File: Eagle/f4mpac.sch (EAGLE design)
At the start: 47 parts, among them CN1 DIP40 MB CONN, IC1 YM2413, IC10 27C128L, IC2 74LS30D, IC3 74LS04D, IC4 LM4558N, IC5 Z80, IC6 74LS30D, IC7 74LS02D, IC8 74LS74D, IC9 74LS125D

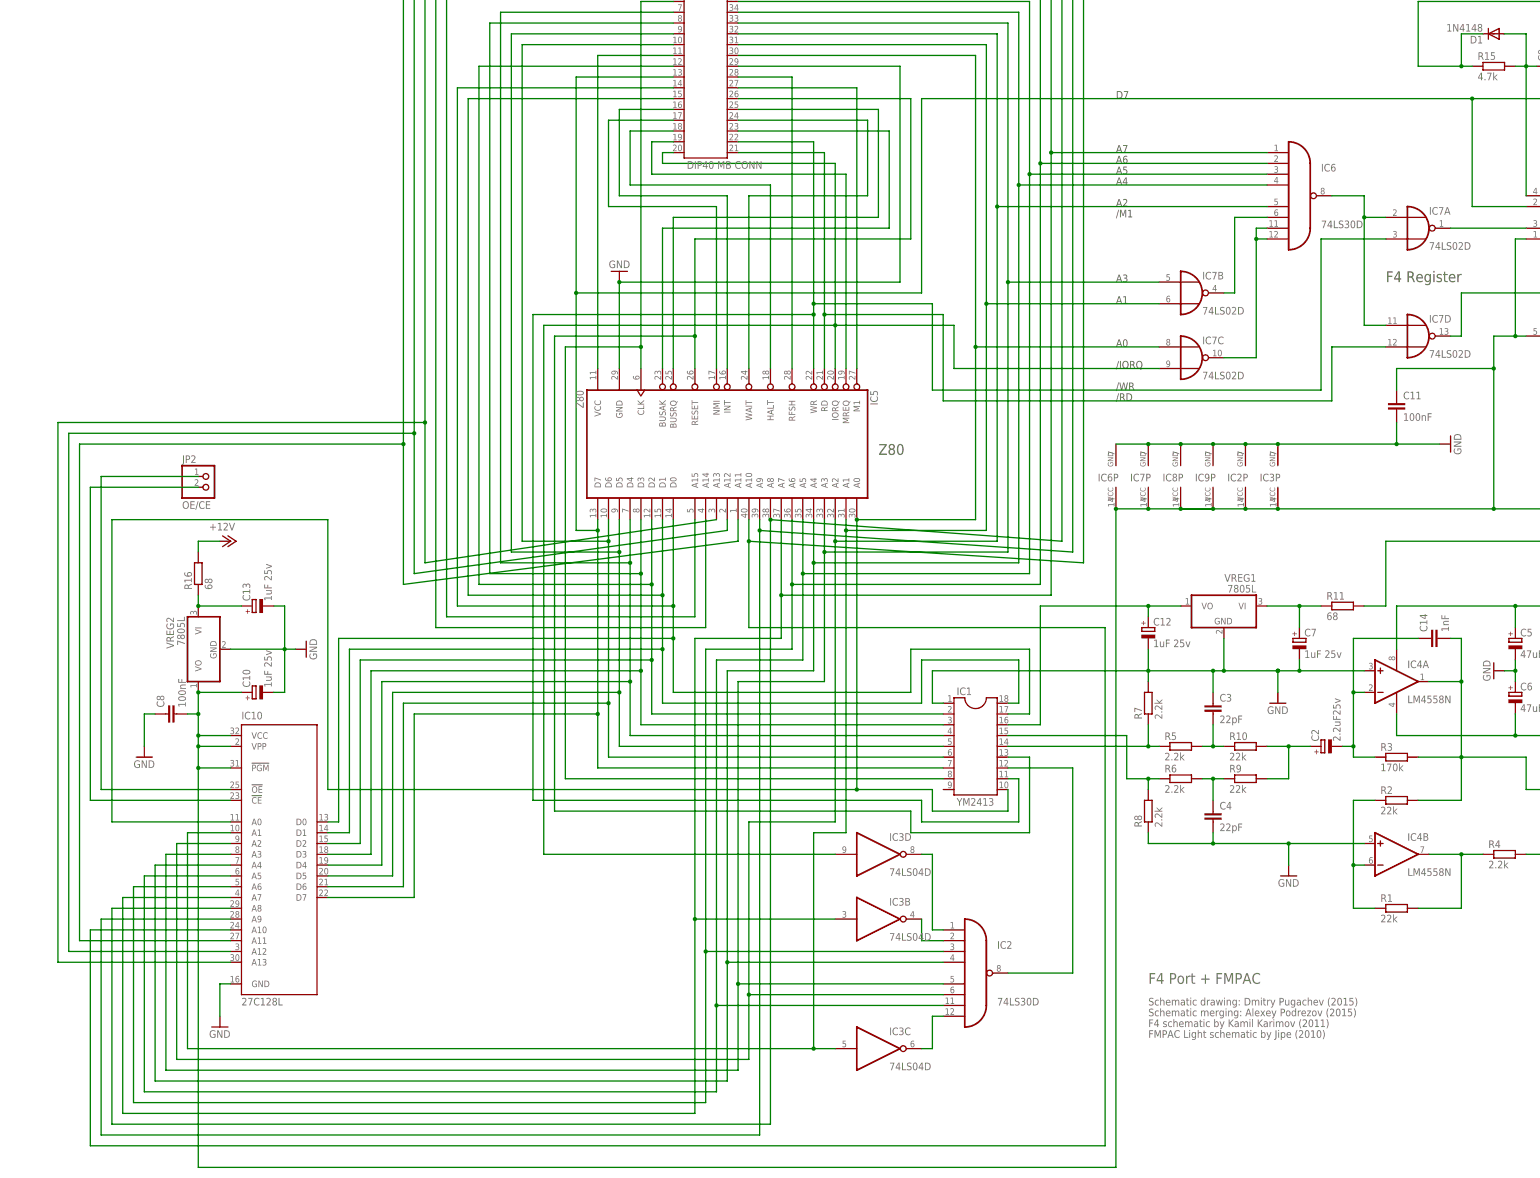
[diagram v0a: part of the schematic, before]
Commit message: New board version 1.3
New board version 1.3, new combined and selectable ROM, easier to get
ROM chip, corrected names error, blocking capacitors, additional noise
suppressing capacitor
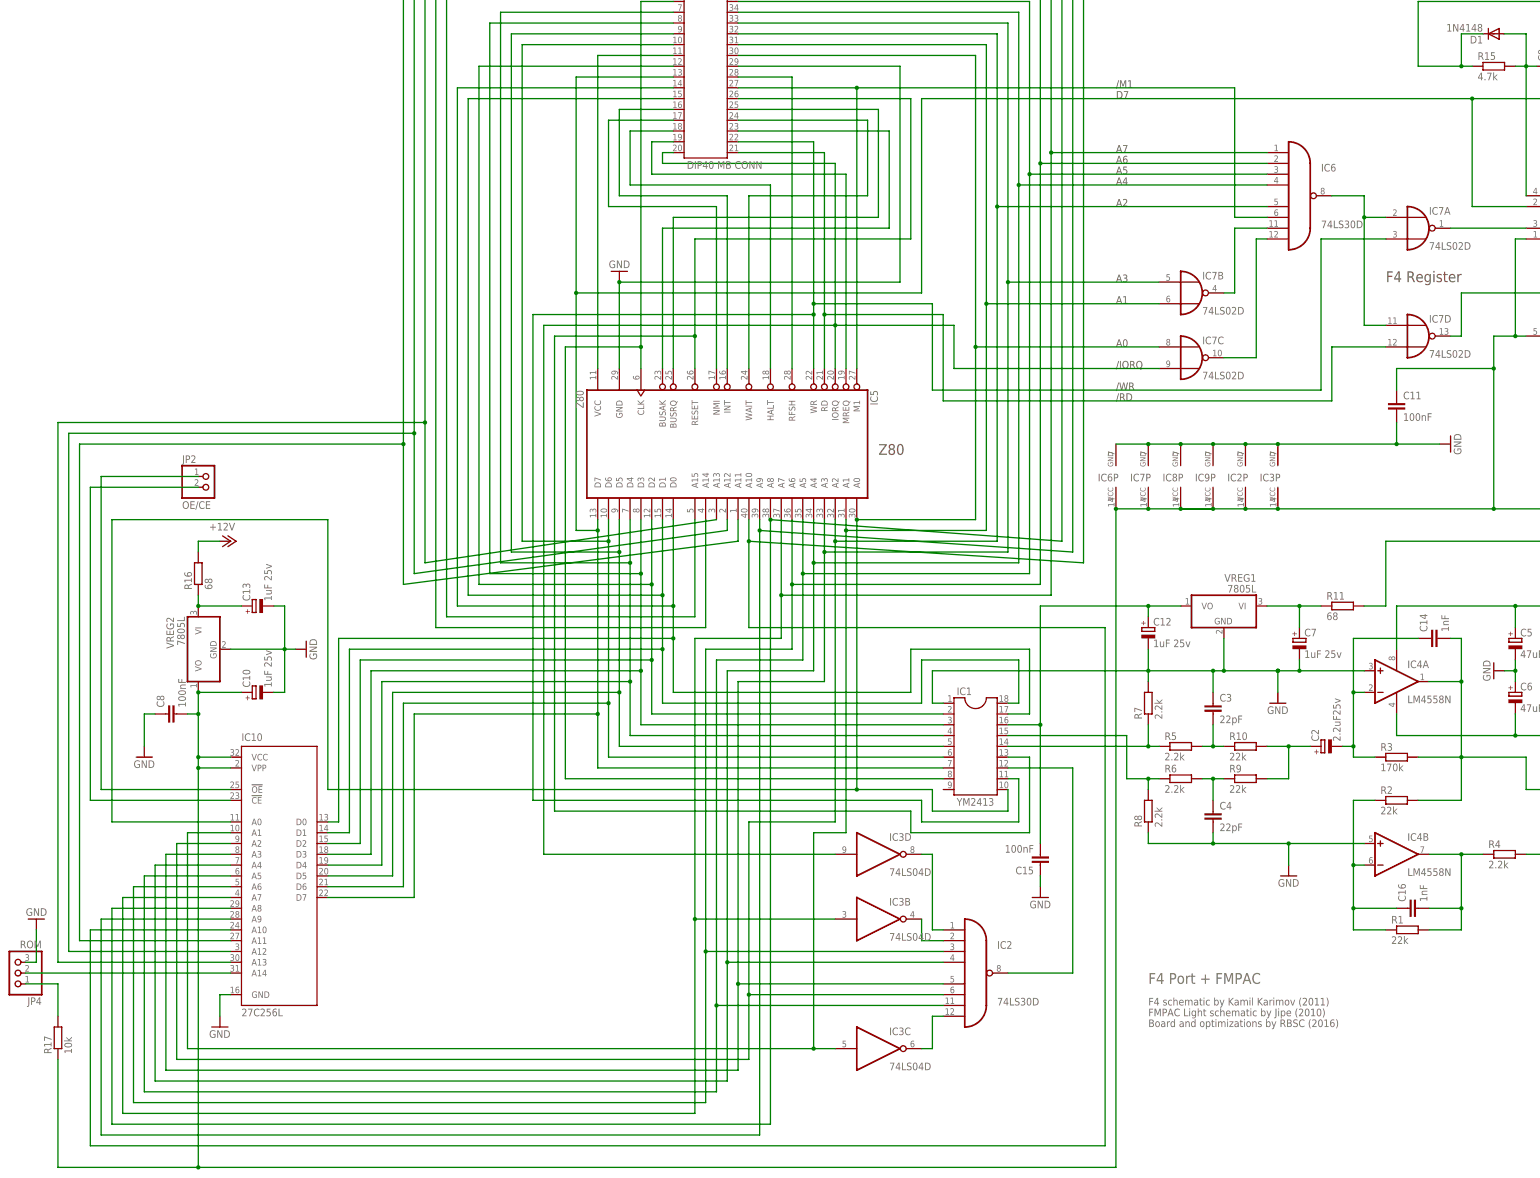
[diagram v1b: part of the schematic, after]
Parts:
- added C15: 100nF, rcl:C-EUC0805
- added C16: 1nF, rcl:C-EUC0805
- added JP4: ROM, pinhead:PINHD-1X3/90
- added R17: 10k, rcl:R-EU_R0805
- IC10: value 27C128L -> 27C256L; device microchip:27C128L -> microchip:27C256L
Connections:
- removed net N$10: IC4B.OUT, R1.2, R4.1
- removed net N$29: IC6A.I5, IC7B.O
- new net N$24: IC6A.I6, IC7B.O
- new net N$25: IC10.A14, JP4.2
- new net N$26: JP4.1, R17.2
- new net N$27: C16.2, IC4B.OUT, R1.2, R4.1
- net +5VREG: now also R17.1; no longer IC10.!PGM
- net GND: now also C15.1, JP4.3
- net M1: now also IC6A.I5
- net N$23: now also C15.2
- net N$30: no longer IC6A.I6
- net N$9: now also C16.1
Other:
- note added: "Board and optimizations by RBSC (2016)"
- note removed: "Schematic drawing: Dmitry Pugachev (2015)"
- note removed: "Schematic merging: Alexey Podrezov (2015)"
- moved on the sheet: IC10, R1

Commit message: Updated source and gerber files, added schematics
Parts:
- added SJ1, SJ2: (no value), jumper:SJ2W
- IC10: value 27C256L -> 27C512AL; device microchip:27C256L -> microchip:27C512AL
- JP4: value ROM -> ROMSEL; device pinhead:PINHD-1X3/90 -> pinhead:PINHD-1X2/90
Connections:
- new net N$10: IC10.A14, SJ1.2
- net +5VREG: now also SJ2.1; no longer IC10.VPP
- net A14: now also SJ1.3
- net A15: now also SJ2.3
- net GND: now also JP4.1; no longer JP4.3
- net N$20: now also IC10.VPP/!OE; no longer IC10.!OE
- net N$25: now also IC10.A15, SJ2.2; no longer IC10.A14, JP4.2
- net N$26: now also JP4.2, SJ1.1; no longer JP4.1
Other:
- moved on the sheet: IC10, R17
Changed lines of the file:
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@@
 <part name="GND12" library="supply1" deviceset="GND" device=""/>
 <part name="C14" library="rcl" deviceset="C-EU" device="C0805" value="1nF"/>
-<part name="IC10" library="microchip" deviceset="27*256" device="L" technology="C"/>
-<part name="R17" library="rcl" deviceset="R-EU_" device="R0805" value="10k"/>
-<part name="JP4" library="pinhead" deviceset="PINHD-1X3" device="/90" value="ROM"/>
-<part name="GND13" library="supply1" deviceset="GND" device=""/>
 <part name="C15" library="rcl" deviceset="C-EU" device="C0805" value="100nF"/>
 <part name="GND14" library="supply1" deviceset="GND" device=""/>
 <part name="C16" library="rcl" deviceset="C-EU" device="C0805" value="1nF"/>
+<part name="IC10" library="microchip" deviceset="27*512A" device="L" technology="C"/>
+<part name="SJ2" library="jumper" deviceset="SJ2W" device=""/>
+<part name="SJ1" library="jumper" deviceset="SJ2W" device=""/>
+<part name="JP4" library="pinhead" deviceset="PINHD-1X2" device="/90" value="ROMSEL"/>
+<part name="GND13" library="supply1" deviceset="GND" device=""/>
+<part name="R17" library="rcl" deviceset="R-EU_" device="R0805" value="10k"/>
 </parts>
 <sheets>
@@
 <instance part="GND12" gate="1" x="-129.54" y="48.26"/>
 <instance part="C14" gate="G$1" x="172.72" y="76.2" rot="R90"/>
-<instance part="IC10" gate="G$1" x="-99.06" y="20.32"/>
-<instance part="R17" gate="G$1" x="-149.86" y="-17.78" rot="R90"/>
-<instance part="JP4" gate="A" x="-160.02" y="-2.54" rot="R180"/>
-<instance part="GND13" gate="1" x="-154.94" y="10.16" rot="R180"/>
 <instance part="C15" gate="G$1" x="81.28" y="22.86" rot="R180"/>
 <instance part="GND14" gate="1" x="81.28" y="15.24"/>
 <instance part="C16" gate="G$1" x="167.64" y="12.7" rot="R90"/>
+<instance part="IC10" gate="G$1" x="-99.06" y="17.78"/>
+<instance part="SJ2" gate="G$1" x="-172.72" y="-17.78" rot="R180"/>
+<instance part="SJ1" gate="G$1" x="-157.48" y="43.18" rot="R180"/>
+<instance part="JP4" gate="G$1" x="-167.64" y="15.24" rot="R180"/>
+<instance part="GND13" gate="1" x="-162.56" y="-7.62"/>
+<instance part="R17" gate="G$1" x="-157.48" y="2.54" rot="R90"/>
 </instances>
 <busses>
@@
 </segment>
 <segment>
-<pinref part="IC10" gate="G$1" pin="GND"/>
-<pinref part="GND10" gate="1" pin="GND"/>
-<wire x1="-109.22" y1="-7.62" x2="-111.76" y2="-7.62" width="0.1524" layer="91"/>
-<wire x1="-111.76" y1="-7.62" x2="-111.76" y2="-12.7" width="0.1524" layer="91"/>
-</segment>
-<segment>
-<pinref part="JP4" gate="A" pin="3"/>
-<wire x1="-157.48" y1="0" x2="-154.94" y2="0" width="0.1524" layer="91"/>
-<wire x1="-154.94" y1="0" x2="-154.94" y2="7.62" width="0.1524" layer="91"/>
-<pinref part="GND13" gate="1" pin="GND"/>
-</segment>
-<segment>
 <pinref part="GND14" gate="1" pin="GND"/>
 <pinref part="C15" gate="G$1" pin="1"/>
 <wire x1="81.28" y1="17.78" x2="81.28" y2="20.32" width="0.1524" layer="91"/>
+</segment>
+<segment>
+<pinref part="IC10" gate="G$1" pin="GND"/>
+<pinref part="GND10" gate="1" pin="GND"/>
+<wire x1="-109.22" y1="-10.16" x2="-111.76" y2="-10.16" width="0.1524" layer="91"/>
+<wire x1="-111.76" y1="-10.16" x2="-111.76" y2="-12.7" width="0.1524" layer="91"/>
+</segment>
+<segment>
+<pinref part="JP4" gate="G$1" pin="1"/>
+<wire x1="-165.1" y1="12.7" x2="-162.56" y2="12.7" width="0.1524" layer="91"/>
+<wire x1="-162.56" y1="12.7" x2="-162.56" y2="-5.08" width="0.1524" layer="91"/>
+<pinref part="GND13" gate="1" pin="GND"/>
 </segment>
 </net>
@@
 <wire x1="0" y1="104.14" x2="0" y2="81.28" width="0.1524" layer="91"/>
 <wire x1="0" y1="81.28" x2="-58.42" y2="81.28" width="0.1524" layer="91"/>
-<wire x1="-58.42" y1="81.28" x2="-58.42" y2="228.6" width="0.1524" layer="91"/>
 <pinref part="CN1" gate="G$1" pin="5"/>
+<wire x1="-58.42" y1="81.28" x2="-58.42" y2="132.08" width="0.1524" layer="91"/>
+<wire x1="-58.42" y1="132.08" x2="-58.42" y2="228.6" width="0.1524" layer="91"/>
 <wire x1="-58.42" y1="228.6" x2="-5.08" y2="228.6" width="0.1524" layer="91"/>
+<wire x1="-58.42" y1="132.08" x2="-172.72" y2="132.08" width="0.1524" layer="91"/>
+<wire x1="-172.72" y1="132.08" x2="-172.72" y2="-12.7" width="0.1524" layer="91"/>
+<junction x="-58.42" y="132.08"/>
+<pinref part="SJ2" gate="G$1" pin="3"/>
 </segment>
 </net>
@@
 <wire x1="2.54" y1="104.14" x2="2.54" y2="78.74" width="0.1524" layer="91"/>
 <wire x1="2.54" y1="78.74" x2="-60.96" y2="78.74" width="0.1524" layer="91"/>
-<wire x1="-60.96" y1="78.74" x2="-60.96" y2="231.14" width="0.1524" layer="91"/>
+<wire x1="-60.96" y1="78.74" x2="-60.96" y2="129.54" width="0.1524" layer="91"/>
 <pinref part="CN1" gate="G$1" pin="4"/>
+<wire x1="-60.96" y1="129.54" x2="-60.96" y2="231.14" width="0.1524" layer="91"/>
 <wire x1="-60.96" y1="231.14" x2="-5.08" y2="231.14" width="0.1524" layer="91"/>
+<wire x1="-60.96" y1="129.54" x2="-152.4" y2="129.54" width="0.1524" layer="91"/>
+<wire x1="-152.4" y1="129.54" x2="-152.4" y2="53.34" width="0.1524" layer="91"/>
+<junction x="-60.96" y="129.54"/>
+<pinref part="SJ1" gate="G$1" pin="3"/>
+<wire x1="-152.4" y1="53.34" x2="-157.48" y2="53.34" width="0.1524" layer="91"/>
+<wire x1="-157.48" y1="53.34" x2="-157.48" y2="48.26" width="0.1524" layer="91"/>
 </segment>
 </net>
@@
 <wire x1="-116.84" y1="-48.26" x2="-116.84" y2="45.72" width="0.1524" layer="91"/>
 <pinref part="VREG2" gate="A1" pin="VO"/>
-<wire x1="-116.84" y1="45.72" x2="-116.84" y2="48.26" width="0.1524" layer="91"/>
-<wire x1="-116.84" y1="48.26" x2="-116.84" y2="58.42" width="0.1524" layer="91"/>
+<wire x1="-116.84" y1="45.72" x2="-116.84" y2="58.42" width="0.1524" layer="91"/>
 <wire x1="-116.84" y1="63.5" x2="-116.84" y2="58.42" width="0.1524" layer="91"/>
 <pinref part="C10" gate="G$1" pin="+"/>
@@
 <junction x="-116.84" y="58.42"/>
 <pinref part="IC10" gate="G$1" pin="VCC"/>
-<wire x1="-116.84" y1="48.26" x2="-109.22" y2="48.26" width="0.1524" layer="91"/>
-<junction x="-116.84" y="48.26"/>
-<pinref part="IC10" gate="G$1" pin="VPP"/>
-<wire x1="-116.84" y1="45.72" x2="-109.22" y2="45.72" width="0.1524" layer="91"/>
+<wire x1="-109.22" y1="45.72" x2="-116.84" y2="45.72" width="0.1524" layer="91"/>
 <junction x="-116.84" y="45.72"/>
+<wire x1="-172.72" y1="-48.26" x2="-157.48" y2="-48.26" width="0.1524" layer="91"/>
+<junction x="-116.84" y="-48.26"/>
+<pinref part="SJ2" gate="G$1" pin="1"/>
+<wire x1="-157.48" y1="-48.26" x2="-116.84" y2="-48.26" width="0.1524" layer="91"/>
+<wire x1="-172.72" y1="-22.86" x2="-172.72" y2="-48.26" width="0.1524" layer="91"/>
 <pinref part="R17" gate="G$1" pin="1"/>
-<wire x1="-116.84" y1="-48.26" x2="-149.86" y2="-48.26" width="0.1524" layer="91"/>
-<wire x1="-149.86" y1="-48.26" x2="-149.86" y2="-22.86" width="0.1524" layer="91"/>
-<junction x="-116.84" y="-48.26"/>
+<wire x1="-157.48" y1="-2.54" x2="-157.48" y2="-48.26" width="0.1524" layer="91"/>
+<junction x="-157.48" y="-48.26"/>
 </segment>
 </net>
@@
 <wire x1="-139.7" y1="114.3" x2="-139.7" y2="40.64" width="0.1524" layer="91"/>
 <wire x1="-139.7" y1="40.64" x2="-109.22" y2="40.64" width="0.1524" layer="91"/>
-<pinref part="IC10" gate="G$1" pin="!OE"/>
+<pinref part="IC10" gate="G$1" pin="VPP/!OE"/>
 </segment>
 </net>
@@
 </segment>
 </net>
-<net name="N$25" class="0">
-<segment>
-<pinref part="IC10" gate="G$1" pin="A14"/>
-<wire x1="-109.22" y1="-2.54" x2="-157.48" y2="-2.54" width="0.1524" layer="91"/>
-<pinref part="JP4" gate="A" pin="2"/>
-</segment>
-</net>
-<net name="N$26" class="0">
-<segment>
-<pinref part="JP4" gate="A" pin="1"/>
-<pinref part="R17" gate="G$1" pin="2"/>
-<wire x1="-157.48" y1="-5.08" x2="-149.86" y2="-5.08" width="0.1524" layer="91"/>
-<wire x1="-149.86" y1="-5.08" x2="-149.86" y2="-12.7" width="0.1524" layer="91"/>
-</segment>
-</net>
 <net name="N$27" class="0">
 <segment>
@@
 </segment>
 </net>
+<net name="N$10" class="0">
+<segment>
+<pinref part="IC10" gate="G$1" pin="A14"/>
+<wire x1="-109.22" y1="-2.54" x2="-152.4" y2="-2.54" width="0.1524" layer="91"/>
+<pinref part="SJ1" gate="G$1" pin="2"/>
+<wire x1="-152.4" y1="-2.54" x2="-152.4" y2="43.18" width="0.1524" layer="91"/>
+</segment>
+</net>
+<net name="N$25" class="0">
+<segment>
+<pinref part="IC10" gate="G$1" pin="A15"/>
+<wire x1="-109.22" y1="-5.08" x2="-152.4" y2="-5.08" width="0.1524" layer="91"/>
+<wire x1="-152.4" y1="-5.08" x2="-152.4" y2="-17.78" width="0.1524" layer="91"/>
+<pinref part="SJ2" gate="G$1" pin="2"/>
+<wire x1="-152.4" y1="-17.78" x2="-167.64" y2="-17.78" width="0.1524" layer="91"/>
+</segment>
+</net>
+<net name="N$26" class="0">
+<segment>
+<pinref part="SJ1" gate="G$1" pin="1"/>
+<wire x1="-157.48" y1="38.1" x2="-157.48" y2="15.24" width="0.1524" layer="91"/>
+<pinref part="JP4" gate="G$1" pin="2"/>
+<wire x1="-165.1" y1="15.24" x2="-157.48" y2="15.24" width="0.1524" layer="91"/>
+<pinref part="R17" gate="G$1" pin="2"/>
+<wire x1="-157.48" y1="7.62" x2="-157.48" y2="15.24" width="0.1524" layer="91"/>
+<junction x="-157.48" y="15.24"/>
+</segment>
+</net>
